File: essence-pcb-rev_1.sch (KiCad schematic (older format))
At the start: 131 parts, among them U1 Elite-C

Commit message: Footprints assigned in schematic
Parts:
- MX-0, MX-10, MX-100, MX-101, MX-102, MX-103, MX-11, MX-110, MX-111, MX-112, MX-113, MX-12, MX-120, MX-121, MX-122, MX-123, MX-13, MX-130, MX-20, MX-21, MX-22, MX-23, MX-30, MX-31, MX-32, MX-33, MX-40, MX-41, MX-42, MX-43, MX-50, MX-51, MX-52, MX-53, MX-60, MX-61, MX-62, MX-70, MX-71, MX-72, MX-80, MX-81, MX-82, MX-83, MX-90, MX-91, MX-92, MX-93: footprint (none) -> MX_Alps_Hybrid:MX-1U-NoLED
- MX-1: footprint (none) -> MX_Alps_Hybrid:MX-1.5U-NoLED
- MX-104, MX-134, MX-34, MX-4, MX-44, MX-94: footprint (none) -> MX_Alps_Hybrid:MX-1.25U-NoLED
- MX-131: footprint (none) -> MX_Alps_Hybrid:MX-2U-NoLED
- MX-132, MX-3: footprint (none) -> MX_Alps_Hybrid:MX-2.25U-NoLED
- MX-133, MX-2: footprint (none) -> MX_Alps_Hybrid:MX-1.75U-NoLED
- MX-54, MX-64, MX-74, MX-84: footprint (none) -> MX_Alps_Hybrid:MX-1.5U-Vertical
- SW1: renamed from SW?; footprint (none) -> Keebio-Parts:RotaryEncoder_Alps_EC11E-Switch_Vertical_H20mm
- U1: footprint (none) -> Keebio-Parts:Elite-C-castellated-29pin-holes
- renumbered D73(Encoder) to D73(Encoder)1

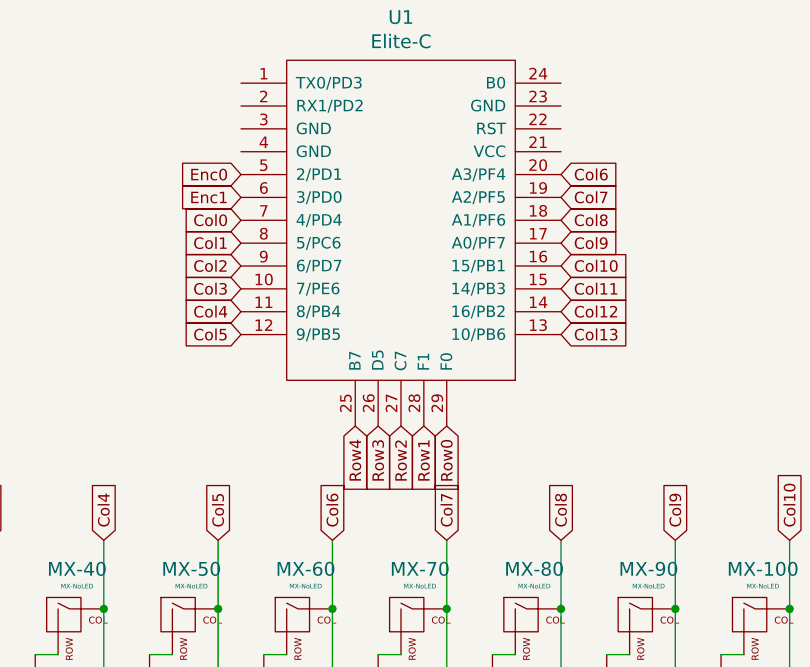
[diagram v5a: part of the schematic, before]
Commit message: Updated pin placement on Elite C to matrix
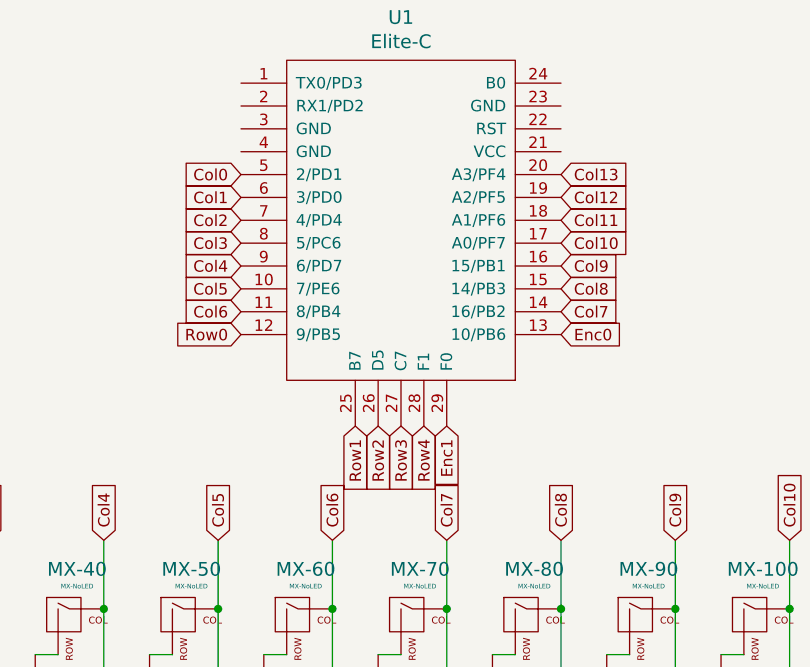
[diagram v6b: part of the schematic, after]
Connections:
- net Col0: now also U1.5 (2/PD1); no longer U1.7 (4/PD4)
- net Col1: now also U1.6 (3/PD0); no longer U1.8 (5/PC6)
- net Col10: now also U1.17 (A0/PF7); no longer U1.16 (15/PB1)
- net Col11: now also U1.18 (A1/PF6); no longer U1.15 (14/PB3)
- net Col12: now also U1.19 (A2/PF5); no longer U1.14 (16/PB2)
- net Col13: now also U1.20 (A3/PF4); no longer U1.13 (10/PB6)
- net Col2: now also U1.7 (4/PD4); no longer U1.9 (6/PD7)
- net Col3: now also U1.8 (5/PC6); no longer U1.10 (7/PE6)
- net Col4: now also U1.9 (6/PD7); no longer U1.11 (8/PB4)
- net Col5: now also U1.10 (7/PE6); no longer U1.12 (9/PB5)
- net Col6: now also U1.11 (8/PB4); no longer U1.20 (A3/PF4)
- net Col7: now also U1.14 (16/PB2); no longer U1.19 (A2/PF5)
- net Col8: now also U1.15 (14/PB3); no longer U1.18 (A1/PF6)
- net Col9: now also U1.16 (15/PB1); no longer U1.17 (A0/PF7)
- net Enc0: now also U1.13 (10/PB6); no longer U1.5 (2/PD1)
- net Enc1: now also U1.29 (F0); no longer U1.6 (3/PD0)
- net Row0: now also U1.12 (9/PB5); no longer U1.29 (F0)
- net Row1: now also U1.25 (B7); no longer U1.28 (F1)
- net Row2: now also U1.26 (D5); no longer U1.27 (C7)
- net Row3: now also U1.27 (C7); no longer U1.26 (D5)
- net Row4: now also U1.28 (F1); no longer U1.25 (B7)
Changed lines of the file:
@@
 Text GLabel 1450 6450 0    50   Input ~ 0
 Row4
+Text GLabel 4600 1250 0    50   Input ~ 0
+Col0
+Text GLabel 4600 1350 0    50   Input ~ 0
+Col1
 Text GLabel 4600 1450 0    50   Input ~ 0
-Col0
+Col2
 Text GLabel 4600 1550 0    50   Input ~ 0
-Col1
+Col3
 Text GLabel 4600 1650 0    50   Input ~ 0
-Col2
+Col4
 Text GLabel 4600 1750 0    50   Input ~ 0
-Col3
+Col5
 Text GLabel 4600 1850 0    50   Input ~ 0
-Col4
+Col6
+Text GLabel 6000 1850 2    50   Input ~ 0
+Col7
+Text GLabel 6000 1750 2    50   Input ~ 0
+Col8
+Text GLabel 6000 1650 2    50   Input ~ 0
+Col9
+Text GLabel 6000 1250 2    50   Input ~ 0
+Col13
+Text GLabel 6000 1350 2    50   Input ~ 0
+Col12
+Text GLabel 6000 1450 2    50   Input ~ 0
+Col11
+Text GLabel 6000 1550 2    50   Input ~ 0
+Col10
 Text GLabel 4600 1950 0    50   Input ~ 0
-Col5
-Text GLabel 6000 1250 2    50   Input ~ 0
-Col6
-Text GLabel 6000 1350 2    50   Input ~ 0
-Col7
-Text GLabel 6000 1450 2    50   Input ~ 0
-Col8
-Text GLabel 6000 1550 2    50   Input ~ 0
-Col9
-Text GLabel 6000 1950 2    50   Input ~ 0
-Col13
-Text GLabel 6000 1850 2    50   Input ~ 0
-Col12
-Text GLabel 6000 1750 2    50   Input ~ 0
-Col11
-Text GLabel 6000 1650 2    50   Input ~ 0
-Col10
-Text GLabel 5500 2350 3    50   Input ~ 0
 Row0
+Text GLabel 5100 2350 3    50   Input ~ 0
+Row1
+Text GLabel 5200 2350 3    50   Input ~ 0
+Row2
+Text GLabel 5300 2350 3    50   Input ~ 0
+Row3
 Text GLabel 5400 2350 3    50   Input ~ 0
-Row1
-Text GLabel 5300 2350 3    50   Input ~ 0
-Row2
-Text GLabel 5200 2350 3    50   Input ~ 0
-Row3
-Text GLabel 5100 2350 3    50   Input ~ 0
 Row4
 Connection ~ 5700 6450
@@
 Wire Wire Line
 	4850 5450 4750 5450
-Text GLabel 4600 1250 0    50   Input ~ 0
+Text GLabel 6000 1950 2    50   Input ~ 0
 Enc0
-Text GLabel 4600 1350 0    50   Input ~ 0
+Text GLabel 5500 2350 3    50   Input ~ 0
 Enc1
 Text GLabel 4750 5350 0    50   Input ~ 0

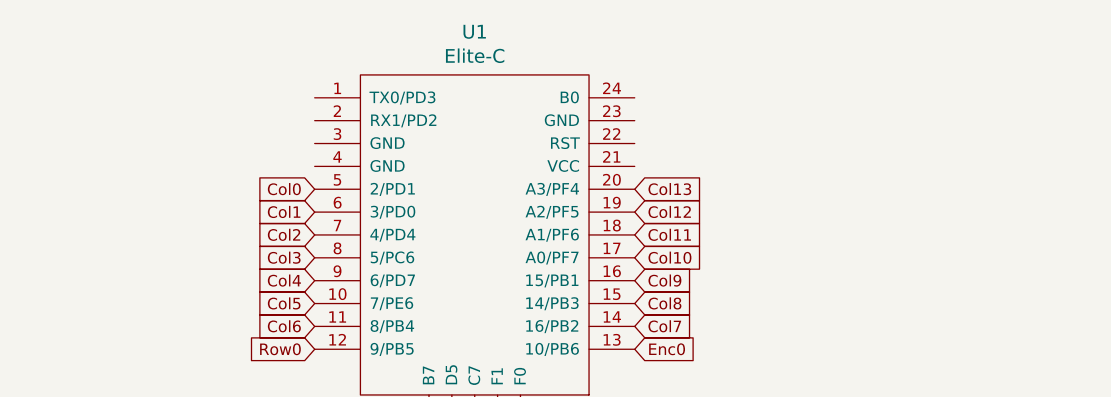
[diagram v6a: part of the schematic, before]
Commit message: Reset Switch added, and Ground fields defined
I think I outlined the ground fields correctly, but I will get input to be sure before I manufacture it
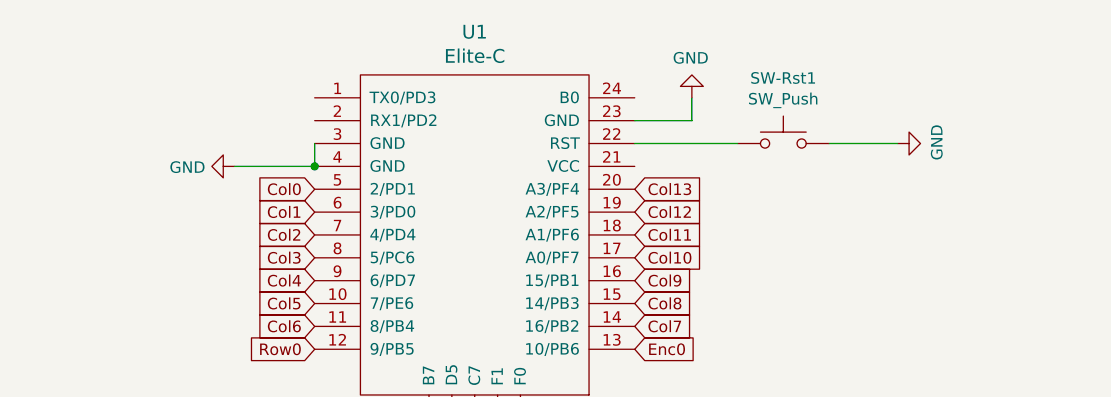
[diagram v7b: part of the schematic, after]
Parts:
- added SW-Rst1: SW_Push, Keebio-Parts:SW_Tactile_SPST_Angled_MJTP1117, symbol Switch:SW_Push
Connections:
- net GND: now also U1.23 (GND), U1.3 (GND), U1.4 (GND), SW-Rst1.2
- net at U1.22 (RST): now also SW-Rst1.1
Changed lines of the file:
@@
 Wire Wire Line
 	4850 5550 4750 5550
+$Comp
+L Switch:SW_Push SW-Rst1
+U 1 1 623849E5
+P 6650 1050
+F 0 "SW-Rst1" H 6650 1335 50  0000 C CNN
+F 1 "SW_Push" H 6650 1244 50  0000 C CNN
+F 2 "Keebio-Parts:SW_Tactile_SPST_Angled_MJTP1117" H 6650 1250 50  0001 C CNN
+F 3 "~" H 6650 1250 50  0001 C CNN
+	1    6650 1050
+	1    0    0    -1
+$EndComp
+Wire Wire Line
+	6000 1050 6450 1050
+Wire Wire Line
+	6850 1050 7150 1050
+$Comp
+L power:GND #PWR0102
+U 1 1 623B74E3
+P 7150 1050
+F 0 "#PWR0102" H 7150 800 50  0001 C CNN
+F 1 "GND" H 7155 877 50  0000 C CNN
+F 2 "" H 7150 1050 50  0001 C CNN
+F 3 "" H 7150 1050 50  0001 C CNN
+	1    7150 1050
+	0    -1   -1   0
+$EndComp
+Wire Wire Line
+	4600 1050 4600 1150
+Wire Wire Line
+	4600 1150 4250 1150
+Connection ~ 4600 1150
+$Comp
+L power:GND #PWR0103
+U 1 1 62401438
+P 4250 1150
+F 0 "#PWR0103" H 4250 900 50  0001 C CNN
+F 1 "GND" V 4255 1022 50  0000 R CNN
+F 2 "" H 4250 1150 50  0001 C CNN
+F 3 "" H 4250 1150 50  0001 C CNN
+	1    4250 1150
+	0    1    1    0
+$EndComp
+Wire Wire Line
+	6000 950  6250 950
+Wire Wire Line
+	6250 950  6250 850
+$Comp
+L power:GND #PWR0104
+U 1 1 62412583
+P 6250 850
+F 0 "#PWR0104" H 6250 600 50  0001 C CNN
+F 1 "GND" H 6255 677 50  0000 C CNN
+F 2 "" H 6250 850 50  0001 C CNN
+F 3 "" H 6250 850 50  0001 C CNN
+	1    6250 850
+	-1   0    0    1
+$EndComp
 $EndSCHEMATC
